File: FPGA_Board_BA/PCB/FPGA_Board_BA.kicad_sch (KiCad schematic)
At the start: 0 parts

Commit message: big schematic cleanup. Added wire to bus
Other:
- sheet ADC for B6 ports: added {ADC_B6}, {Voltage_Current_B6}; removed CLK_IN, CLK_OUT, I_A, I_B, I_C, SDO1, SDO2, SDO3, SDO4, SDO5, SDO6, SDO7, SDO8, V_A, V_B, V_C, V_DC, ~{CNV}
- sheet ADC for Machine ports: added {ADC_Current_Machine}, {ADC_Machine}, {Voltages_Machine}; removed CLK_IN_1, CLK_OUT_1, Iin_1, Iin_2, Iin_3, Iin_4, SDO1_1, SDO2_1, SDO3_1, SDO4_1, SDO5_1, SDO6_1, SDO7_1, SDO8_1, Vout1+, Vout1-, Vout2+, Vout2-, Vout3+, Vout3-, Vout4+, Vout4-, ~{CNV}_1
- sheet CHB Communication ports: added {Enable_Lines}, {Error_Lines}, {Rx_Lines}; removed Ph_A_En, Ph_A_Err, Ph_A_Rx, Ph_B_En, Ph_B_Err, Ph_B_Rx, Ph_C_En, Ph_C_Err, Ph_C_Rx, Ph_D_En, Ph_D_Err, Ph_D_Rx
- sheet Current measure ports: added {ADC_Current_Machine}; removed PHA, PHB, PHC, PHD
- sheet Encoder ports: added {Encoder}; removed ENC_A, ENC_B, ENC_I
- sheet FPGA ports: added {ADC_B6}, {ADC_Machine}, {B6_Control}, {Enable_Lines}, {Encoder}, {Error_Lines}, {Rx_Lines}; removed B6_En, CLK_IN, CLK_IN_1, CLK_OUT, CLK_OUT_1, ENC_A_in, ENC_B_in, ENC_I_in, PWM_AH, PWM_AL, PWM_BH, PWM_BL, PWM_CH, PWM_CL, Ph_A_En, Ph_A_Err, Ph_A_Rx, Ph_B_En, Ph_B_Err, Ph_B_Rx, Ph_C_En, Ph_C_Err, Ph_C_Rx, Ph_D_En, Ph_D_Err, Ph_D_Rx, SDO1, SDO1_1, SDO2, SDO2_1, SDO3, SDO3_1, SDO4, SDO4_1, SDO5, SDO5_1, SDO6, SDO6_1, SDO7, SDO7_1, SDO8, SDO8_1, ~{CNV}, ~{CNV}_1
- sheet TI-B6 ports: added {B6_Control}, {Voltage_Current_B6}; removed B6_En, I_A, I_B, I_C, PWM_AH, PWM_AL, PWM_BH, PWM_BL, PWM_CH, PWM_CL, V_A, V_B, V_C, V_DC
- sheet Voltage Measure ports: added {Voltages_Machine}; removed Vout1+, Vout1-, Vout2+, Vout2-, Vout3+, Vout3-, Vout4+, Vout4-

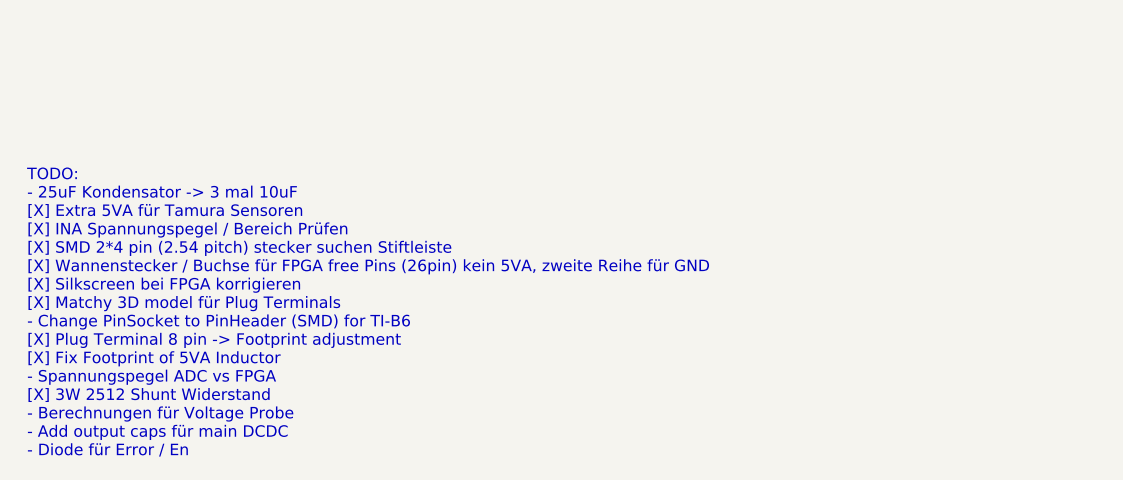
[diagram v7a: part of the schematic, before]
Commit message: PCB left side almost finished + some optimization in schematics
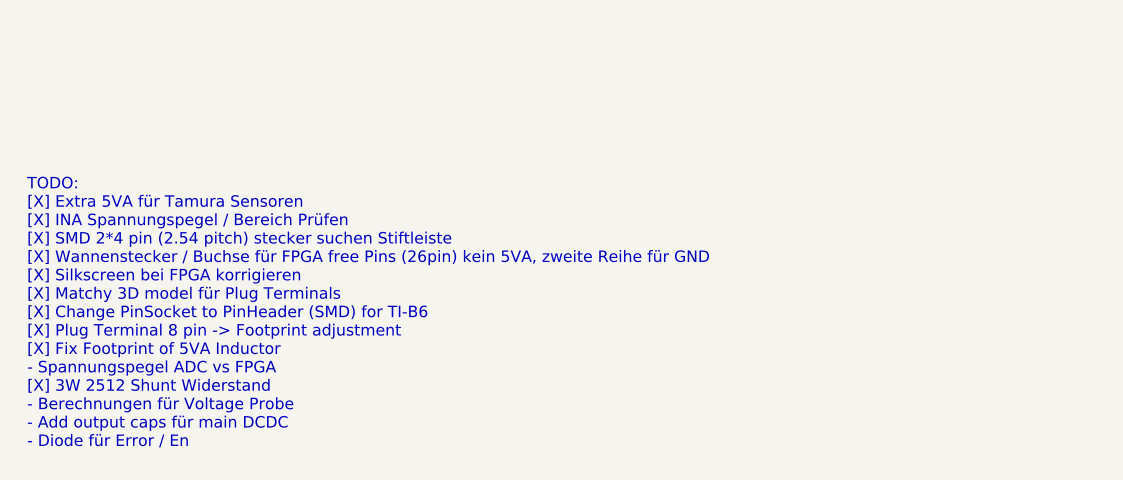
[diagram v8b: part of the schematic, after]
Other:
- note added: "TODO: [X] Extra 5VA für Tamura Sensoren [X] INA Spannungspegel / Bereich Prüfen [X] SMD 2*4 pin (2.54 pitch) stecker suchen Stiftleiste [X] Wannenstecker / Buchse für FPGA free Pins (26pin) kein 5VA, zweite Reihe für GND [X] Silkscreen bei FPGA korrigieren [X] Matchy 3D model für Plug Terminals [X] Change PinSocket to PinHeader (SMD) for TI-B6 [X] Plug Terminal 8 pin -> Footprint adjustment [X] F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"
- note removed: "TODO: - 25uF Kondensator -> 3 mal 10uF [X] Extra 5VA für Tamura Sensoren [X] INA Spannungspegel / Bereich Prüfen [X] SMD 2*4 pin (2.54 pitch) stecker suchen Stiftleiste [X] Wannenstecker / Buchse für FPGA free Pins (26pin) kein 5VA, zweite Reihe für GND [X] Silkscreen bei FPGA korrigieren [X] Matchy 3D model für Plug Terminals - Change PinSocket to PinHeader (SMD) for TI-B6 [X] Plug Terminal 8 pi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"
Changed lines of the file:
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@@
 	(paper "A4")
 	(bus_alias "ADC_Machine"
-		(members "SDO1" "SDO2" "SDO3" "SDO4" "SDO5" "SDO6" "SDO7" "SDO8" "CLK_OUT"
-			"CLK_IN" "~{CNV}"
+		(members "SDO1_1" "SDO2_1" "SDO3_1" "SDO4_1" "SDO5_1" "SDO6_1" "SDO7_1"
+			"SDO8_1" "CLK_OUT_1" "CLK_IN_1" "~{CNV}_1"
 		)
 	)
-	(text "TODO:\n- 25uF Kondensator -> 3 mal 10uF \n[X] Extra 5VA für Tamura Sensoren\n[X] INA Spannungspegel / Bereich Prüfen\n[X] SMD 2*4 pin (2.54 pitch) stecker suchen Stiftleiste\n[X] Wannenstecker / Buchse für FPGA free Pins (26pin) kein 5VA, zweite Reihe für GND\n[X] Silkscreen bei FPGA korrigieren\n[X] Matchy 3D model für Plug Terminals\n- Change PinSocket to PinHeader (SMD) for TI-B6\n[X] Plug Terminal 8 pin -> Footprint adjustment\n[X] Fix Footprint of 5VA Inductor\n- Spannungspegel ADC vs FPGA\n[X] 3W 2512 Shunt Widerstand\n- Berechnungen für Voltage Probe\n- Add output caps für main DCDC\n- Diode für Error / En"
+	(text "TODO:\n[X] Extra 5VA für Tamura Sensoren\n[X] INA Spannungspegel / Bereich Prüfen\n[X] SMD 2*4 pin (2.54 pitch) stecker suchen Stiftleiste\n[X] Wannenstecker / Buchse für FPGA free Pins (26pin) kein 5VA, zweite Reihe für GND\n[X] Silkscreen bei FPGA korrigieren\n[X] Matchy 3D model für Plug Terminals\n[X] Change PinSocket to PinHeader (SMD) for TI-B6\n[X] Plug Terminal 8 pin -> Footprint adjustment\n[X] Fix Footprint of 5VA Inductor\n- Spannungspegel ADC vs FPGA\n[X] 3W 2512 Shunt Widerstand\n- Berechnungen für Voltage Probe\n- Add output caps für main DCDC\n- Diode für Error / En"
 		(exclude_from_sim no)
 		(at 24.892 171.196 0)
